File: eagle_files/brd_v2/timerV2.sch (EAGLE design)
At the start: 46 parts, among them IC1 7805T, IC6 DS1307, U1 ATMEGA328P

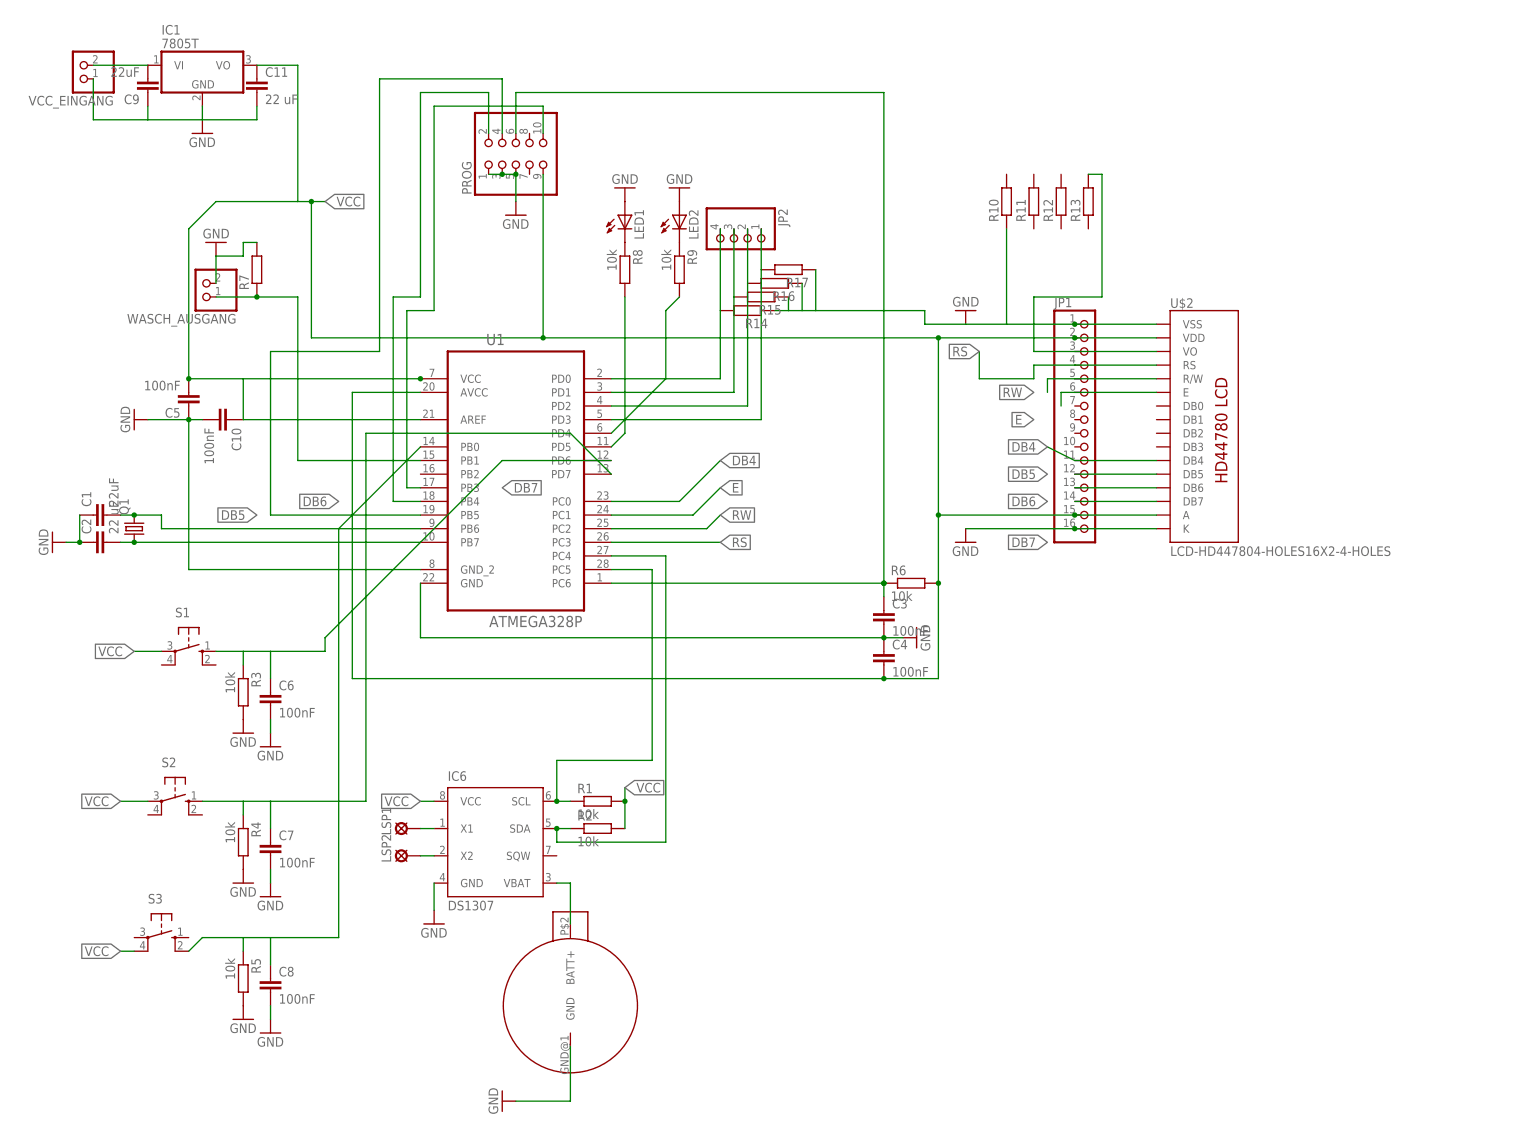
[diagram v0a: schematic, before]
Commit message: added more input pins removed voltage regulator added pinheader
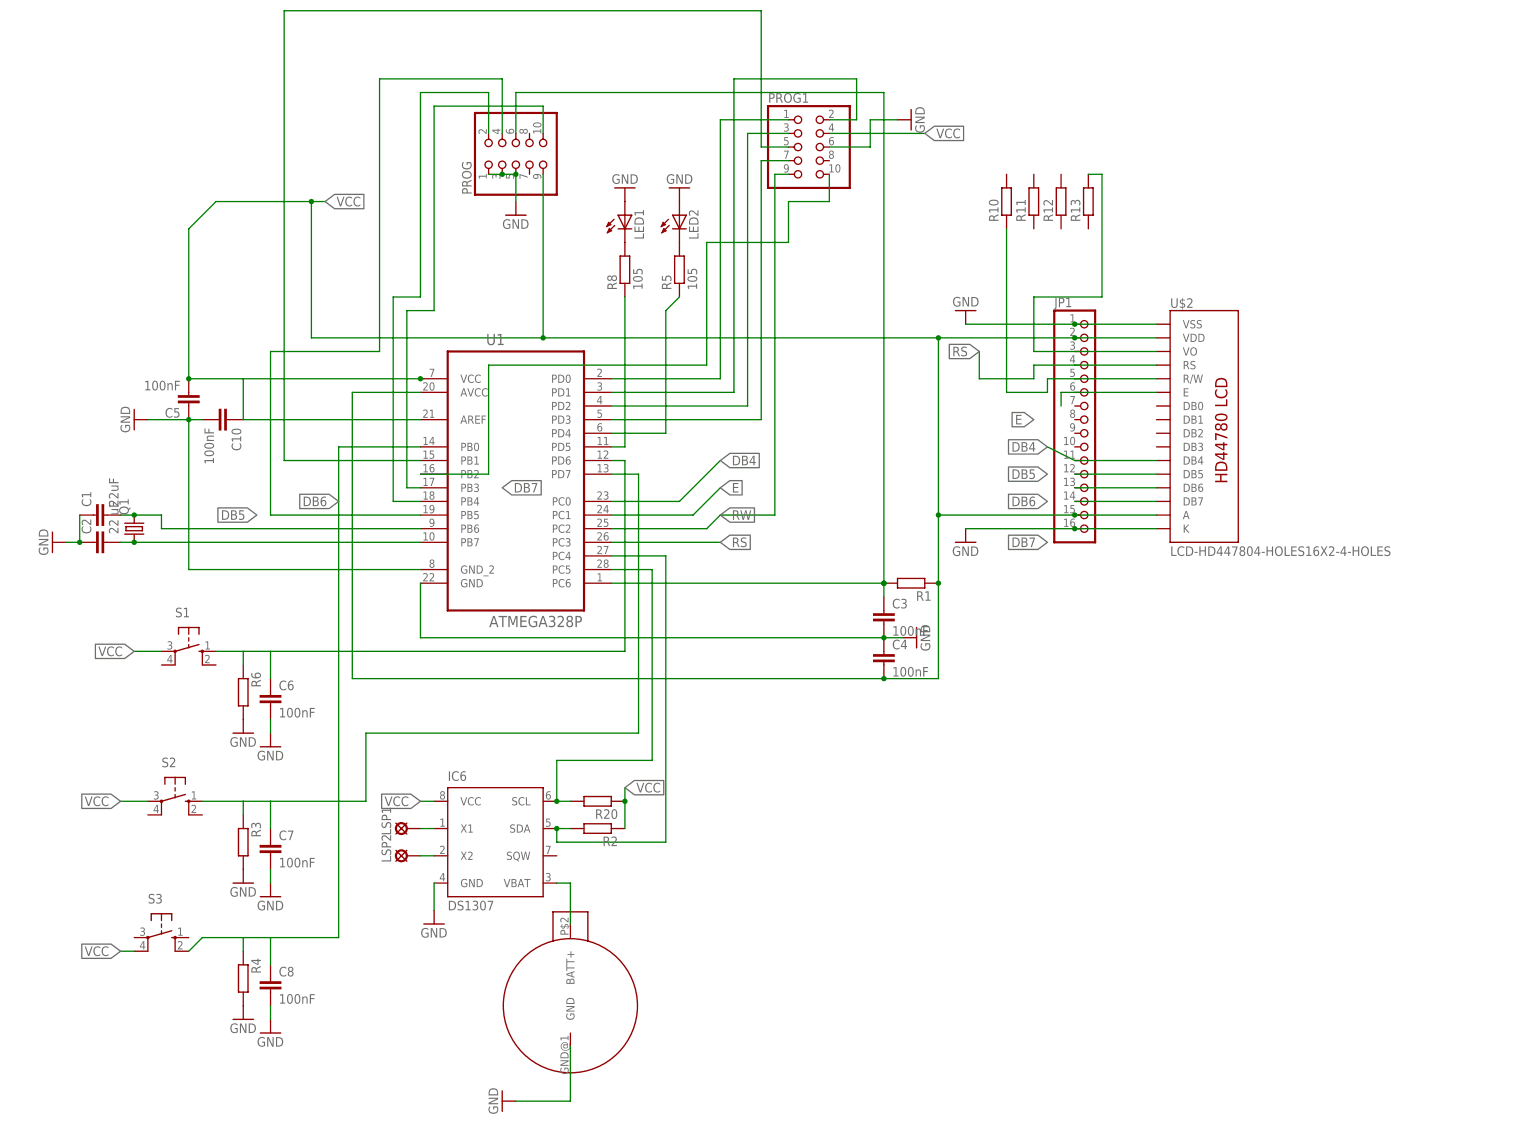
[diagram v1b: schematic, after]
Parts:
- removed C11: 22 uF, resistor:C-EU025-025X050
- removed C9: 22uF, resistor:C-EU025-025X050
- removed IC1: 7805T, linear:7805T
- removed JP2: (no value), pinhead:PINHD-1X4/90
- removed R14, R15, R16, R17, R7: (no value), eagle-ltspice:RR0603
- removed R9: 10k, resistor:R-EU_0204/7
- removed VCC_EINGANG, WASCH_AUSGANG: (no value), pinhead:PINHD-1X2
- added PROG1: (no value), pinhead:PINHD-2X5
- added R20: (no value), eagle-ltspice:RR0603
- R1, R2, R3, R4, R6: value 10k -> (none); device resistor:R-EU_0204/7 -> eagle-ltspice:RR0603
- R5, R8: value 10k -> 105; device resistor:R-EU_0204/7 -> eagle-ltspice:RR0603
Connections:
- removed net N$7: C9.2, IC1.VI, VCC_EINGANG.2
- new net N$6: PROG1.10, U1.PB2
- net GND: now also JP1.5, PROG1.6, R6.2, U$2.R/W; no longer C11.2, C9.1, IC1.GND, R14.1, R15.1, R16.1, R17.1, R5.2, R7.2, VCC_EINGANG.1, WASCH_AUSGANG.2
- net N$1: now also LED2.C, R5.2; no longer LED1.C, R8.1
- net N$11: now also R4.1; no longer R5.1
- net N$12: now also PROG1.7; no longer JP2.1, R17.2
- net N$13: now also R8.1; no longer R8.2
- net N$14: now also R5.1; no longer R9.2
- net N$15: now also PROG1.1; no longer JP2.4, R14.2
- net N$17: now also PROG1.3; no longer JP2.2, R16.2
- net N$20: now also R6.1; no longer R3.1
- net N$3: now also PROG1.5; no longer R7.1, WASCH_AUSGANG.1
- net N$39: now also R20.2; no longer R1.1
- net N$4: now also LED1.C, R8.2; no longer LED2.C, R9.1
- net N$40: now also R2.2; no longer R2.1
- net N$5: now also R1.2; no longer R6.1
- net N$8: now also R3.1; no longer R4.1
- net N$9: now also PROG1.2; no longer JP2.3, R15.2
- net RW: now also PROG1.9; no longer JP1.5, U$2.R/W
- net VCC: now also PROG1.4, R1.1, R2.1, R20.1; no longer C11.1, IC1.VO, R1.2, R2.2, R6.2
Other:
- moved on the sheet: R1, R2, R3, R4, R5, R6, R8

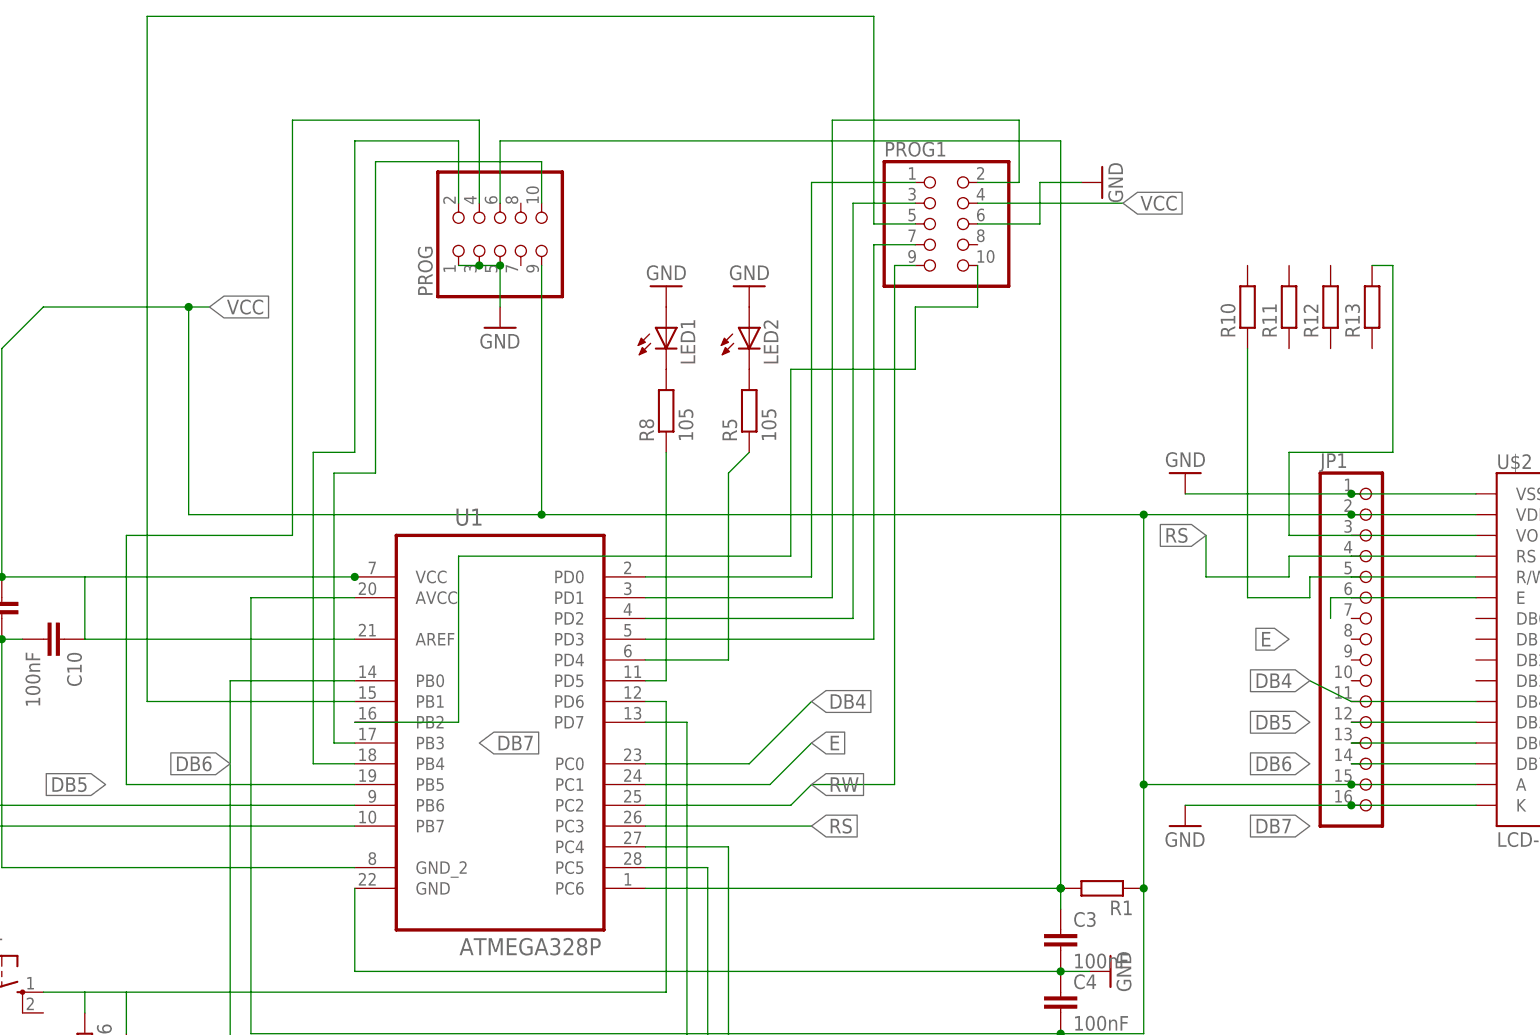
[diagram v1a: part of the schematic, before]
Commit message: Added Pulldown resistors for input pins
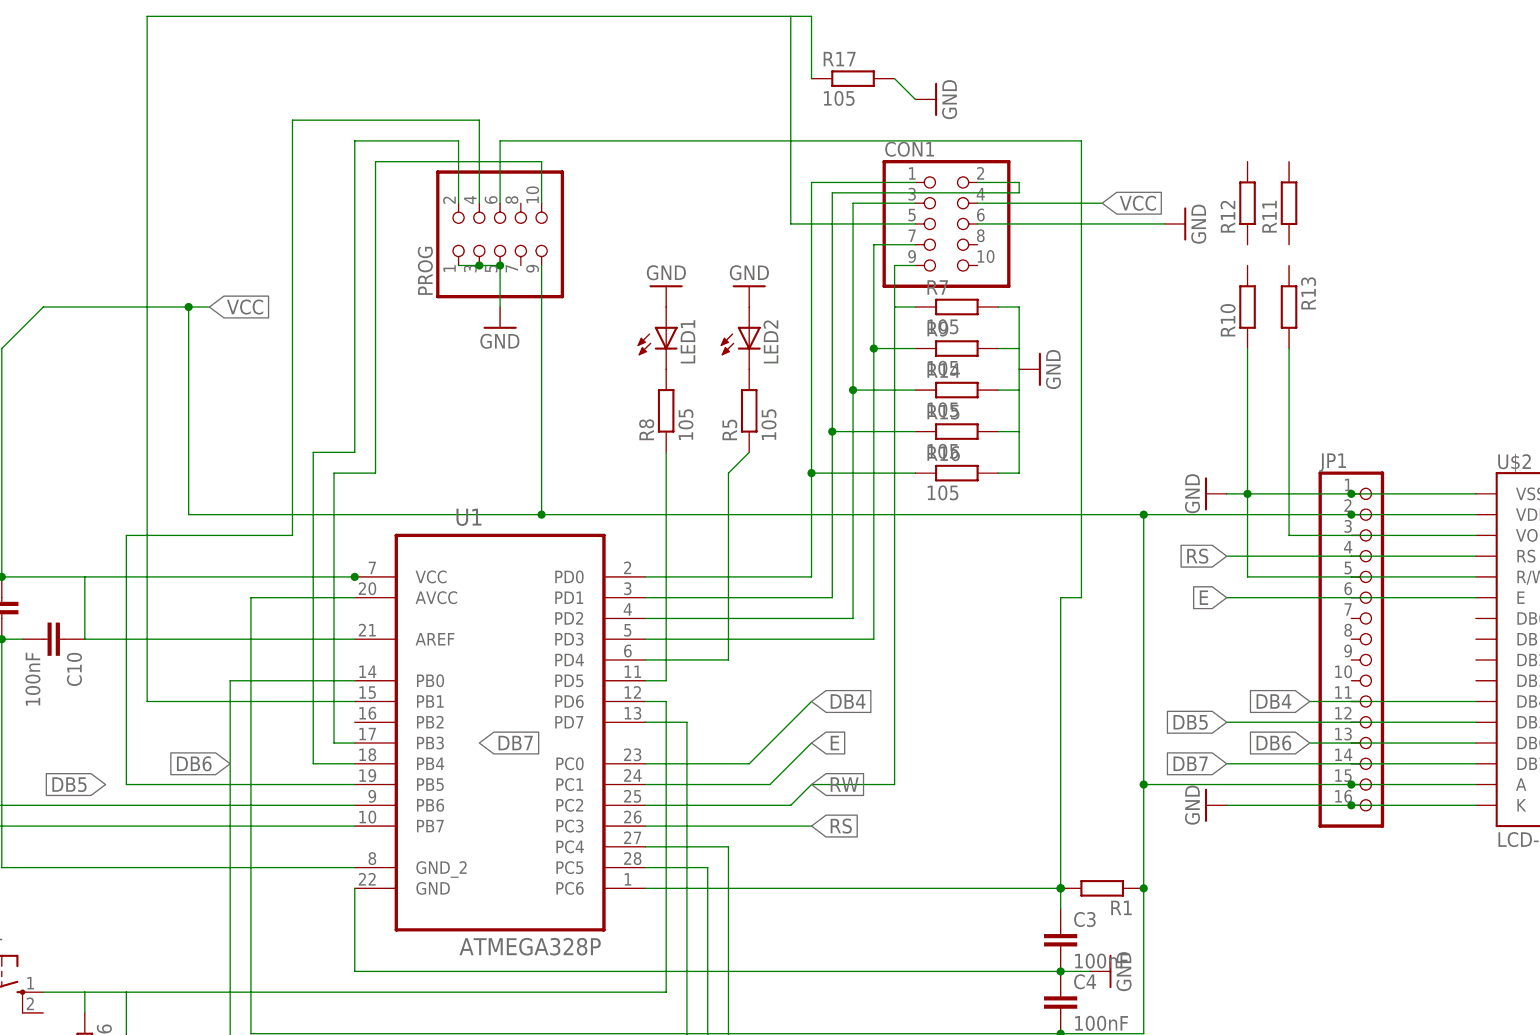
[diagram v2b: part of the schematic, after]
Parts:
- added R14, R15, R16, R17, R7, R9: 105, eagle-ltspice:RR0603
- renumbered PROG1 to CON1
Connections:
- removed net N$6: CON1.10, U1.PB2
- net GND: now also R14.2, R15.2, R16.2, R17.2, R7.2, R9.2
- net N$12: now also R9.1
- net N$15: now also R16.1
- net N$17: now also R14.1
- net N$3: now also R17.1
- net N$9: now also R15.1
- net RW: now also R7.1
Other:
- moved on the sheet: R11, R12, R13

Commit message: added pullup resistors ...
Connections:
- net GND: no longer R14.2, R15.2, R16.2, R7.2, R9.2
- net VCC: now also R14.2, R15.2, R16.2, R7.2, R9.2
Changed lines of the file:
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@@
 <?xml version="1.0" encoding="utf-8"?>
 <!DOCTYPE eagle SYSTEM "eagle.dtd">
-<eagle version="6.5.0">
+<eagle version="6.4">
 <drawing>
 <settings>
@@
 <part name="CON1" library="pinhead" deviceset="PINHD-2X5" device=""/>
 <part name="R7" library="eagle-ltspice" deviceset="R" device="R0603" value="105"/>
-<part name="GND4" library="supply1" deviceset="GND" device=""/>
 <part name="R9" library="eagle-ltspice" deviceset="R" device="R0603" value="105"/>
 <part name="R14" library="eagle-ltspice" deviceset="R" device="R0603" value="105"/>
@@
 <instance part="CON1" gate="A" x="-10.16" y="154.94"/>
 <instance part="R7" gate="G$1" x="-7.62" y="144.78"/>
-<instance part="GND4" gate="1" x="2.54" y="137.16" rot="R90"/>
 <instance part="R9" gate="G$1" x="-7.62" y="139.7"/>
 <instance part="R14" gate="G$1" x="-7.62" y="134.62"/>
@@
 <pinref part="CON1" gate="A" pin="6"/>
 <wire x1="17.78" y1="154.94" x2="-5.08" y2="154.94" width="0.1524" layer="91"/>
-</segment>
-<segment>
-<pinref part="R7" gate="G$1" pin="2"/>
-<pinref part="GND4" gate="1" pin="GND"/>
-<wire x1="-2.54" y1="144.78" x2="0" y2="144.78" width="0.1524" layer="91"/>
-<wire x1="0" y1="144.78" x2="0" y2="139.7" width="0.1524" layer="91"/>
-<pinref part="R9" gate="G$1" pin="2"/>
-<wire x1="0" y1="139.7" x2="0" y2="137.16" width="0.1524" layer="91"/>
-<wire x1="-2.54" y1="139.7" x2="0" y2="139.7" width="0.1524" layer="91"/>
-<pinref part="R14" gate="G$1" pin="2"/>
-<wire x1="-2.54" y1="134.62" x2="0" y2="134.62" width="0.1524" layer="91"/>
-<wire x1="0" y1="134.62" x2="0" y2="137.16" width="0.1524" layer="91"/>
-<pinref part="R15" gate="G$1" pin="2"/>
-<wire x1="-2.54" y1="129.54" x2="0" y2="129.54" width="0.1524" layer="91"/>
-<wire x1="0" y1="129.54" x2="0" y2="134.62" width="0.1524" layer="91"/>
-<pinref part="R16" gate="G$1" pin="2"/>
-<wire x1="-2.54" y1="124.46" x2="0" y2="124.46" width="0.1524" layer="91"/>
-<wire x1="0" y1="124.46" x2="0" y2="129.54" width="0.1524" layer="91"/>
 </segment>
 <segment>
@@
 <pinref part="CON1" gate="A" pin="4"/>
 </segment>
+<segment>
+<pinref part="R7" gate="G$1" pin="2"/>
+<wire x1="-2.54" y1="144.78" x2="0" y2="144.78" width="0.1524" layer="91"/>
+<wire x1="0" y1="144.78" x2="0" y2="139.7" width="0.1524" layer="91"/>
+<pinref part="R9" gate="G$1" pin="2"/>
+<wire x1="-2.54" y1="139.7" x2="0" y2="139.7" width="0.1524" layer="91"/>
+<pinref part="R14" gate="G$1" pin="2"/>
+<wire x1="-2.54" y1="134.62" x2="0" y2="134.62" width="0.1524" layer="91"/>
+<wire x1="0" y1="134.62" x2="0" y2="139.7" width="0.1524" layer="91"/>
+<pinref part="R15" gate="G$1" pin="2"/>
+<wire x1="-2.54" y1="129.54" x2="0" y2="129.54" width="0.1524" layer="91"/>
+<wire x1="0" y1="129.54" x2="0" y2="134.62" width="0.1524" layer="91"/>
+<pinref part="R16" gate="G$1" pin="2"/>
+<wire x1="-2.54" y1="124.46" x2="0" y2="124.46" width="0.1524" layer="91"/>
+<wire x1="0" y1="124.46" x2="0" y2="129.54" width="0.1524" layer="91"/>
+<label x="0" y="144.78" size="1.778" layer="95" xref="yes"/>
+</segment>
 </net>
